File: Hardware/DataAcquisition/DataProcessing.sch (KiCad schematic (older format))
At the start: 36 parts, among them J1 Conn_01x04_Female, J2 Conn_01x04_Female, U5 STM32F030K6Tx, Y1 20MHz

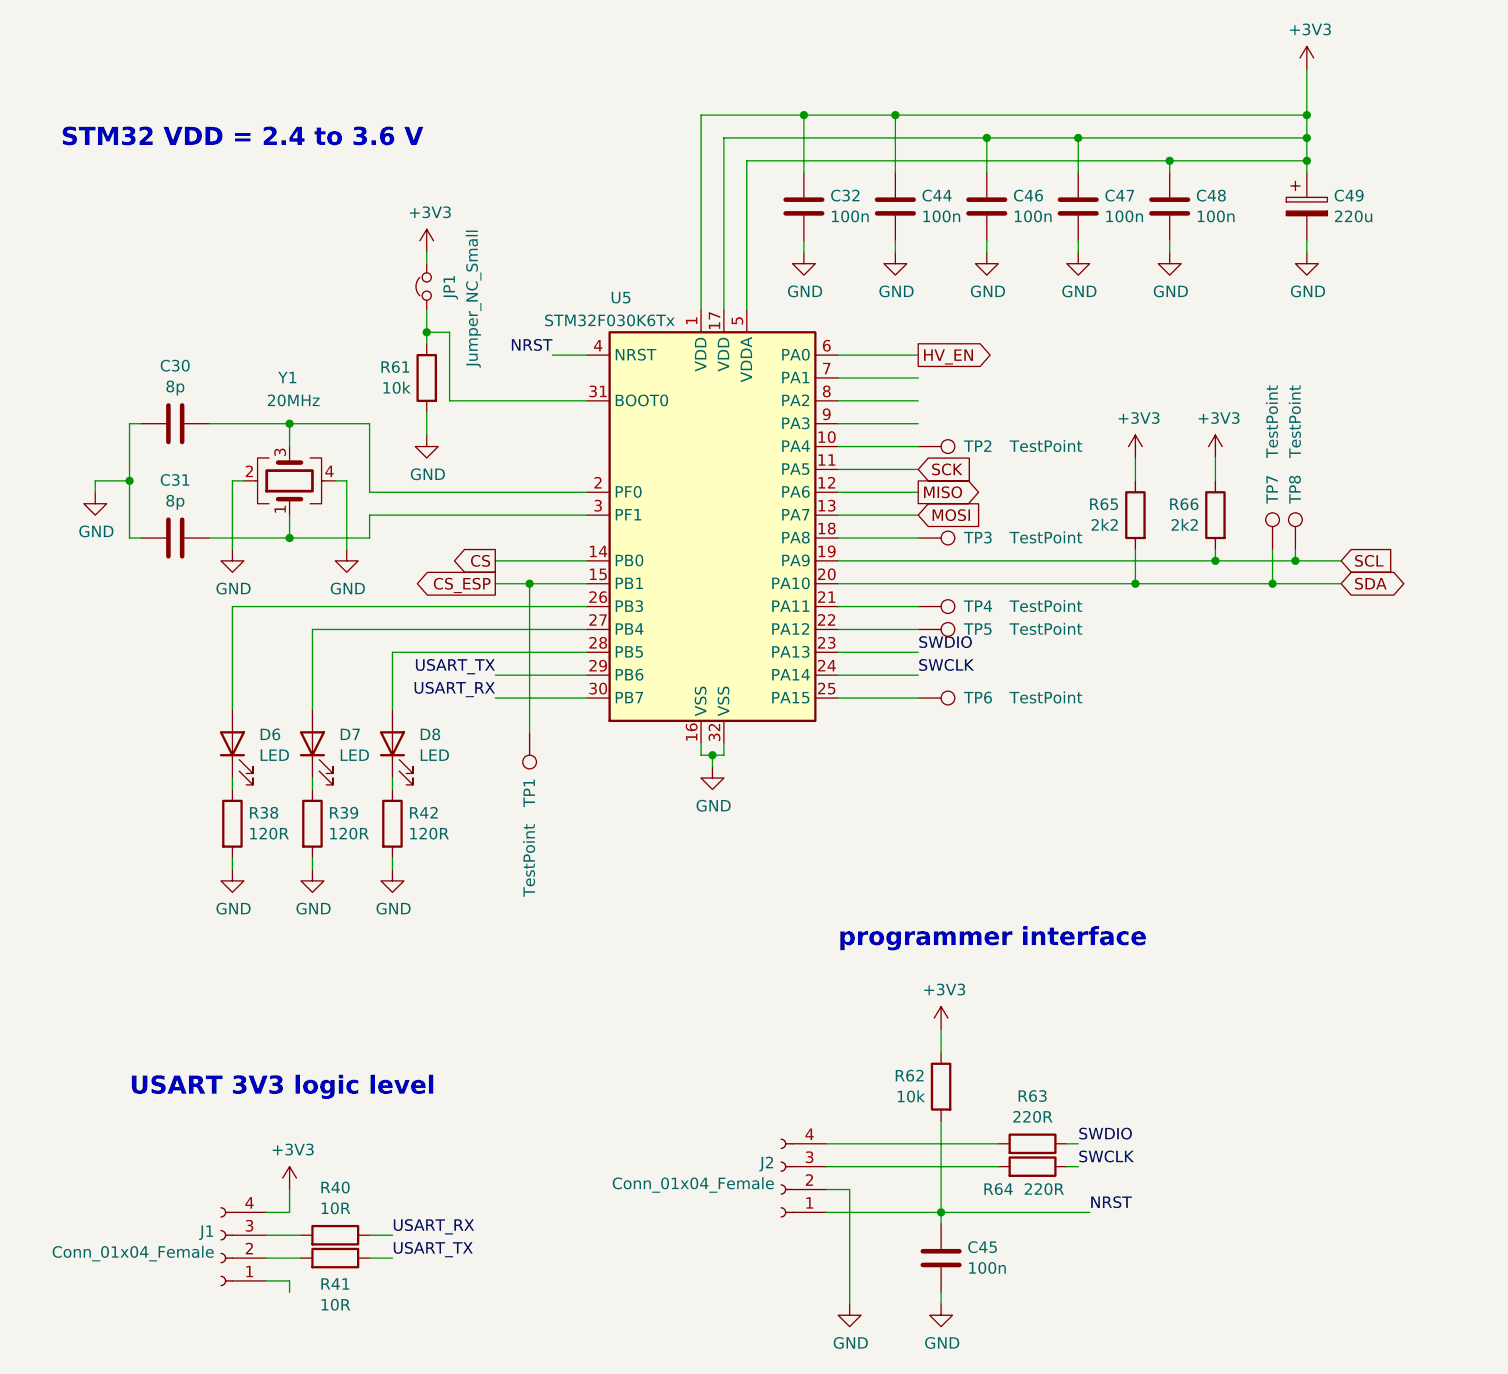
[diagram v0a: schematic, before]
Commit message: split (previousle one) pcb project to three separate pcbs
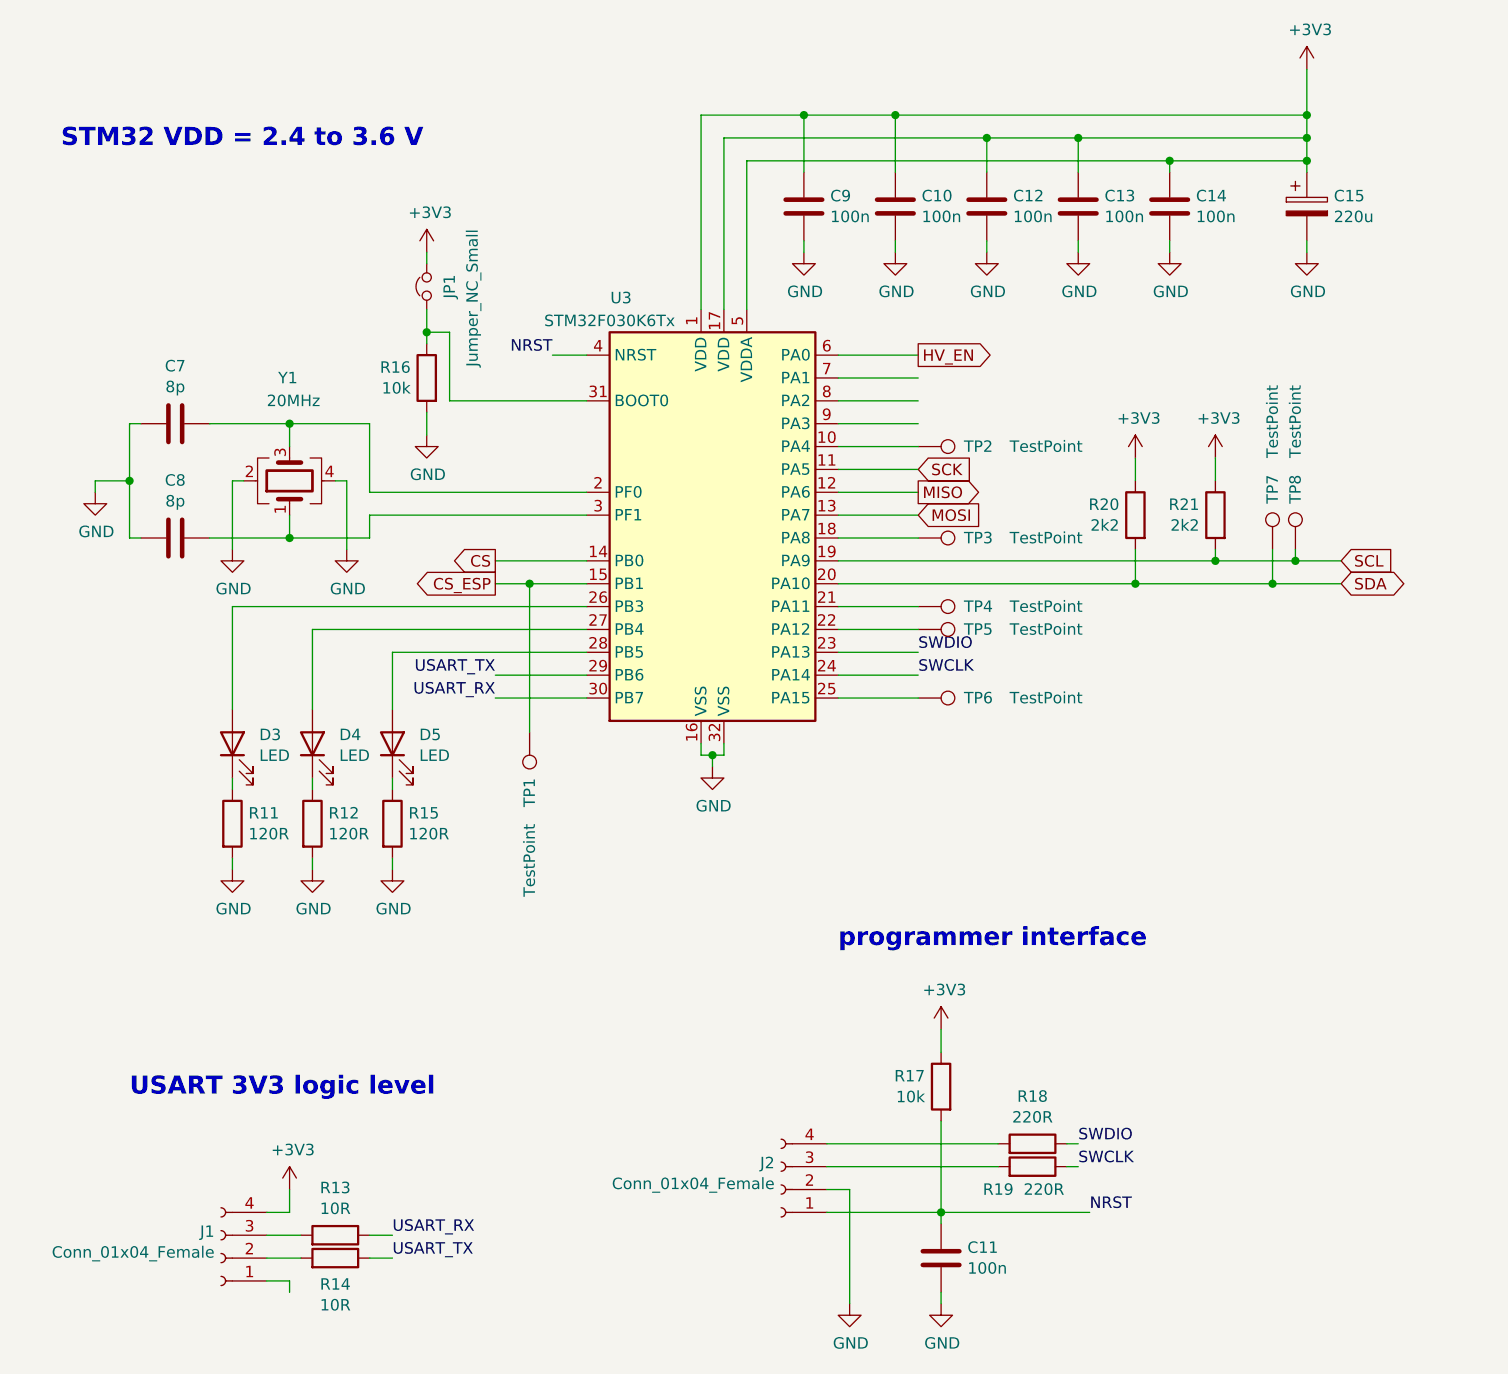
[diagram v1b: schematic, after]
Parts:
- renumbered C44 to C10, C45 to C11, C46 to C12, C47 to C13, C48 to C14, C49 to C15, C30 to C7, C31 to C8, C32 to C9, D6 to D3, D7 to D4, D8 to D5, R38 to R11, R39 to R12, R40 to R13, R41 to R14, R42 to R15, R61 to R16, R62 to R17, R63 to R18, R64 to R19, R65 to R20, R66 to R21, U5 to U3

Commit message: Clarify architecture of acquisition module (#80), removed obsolete files
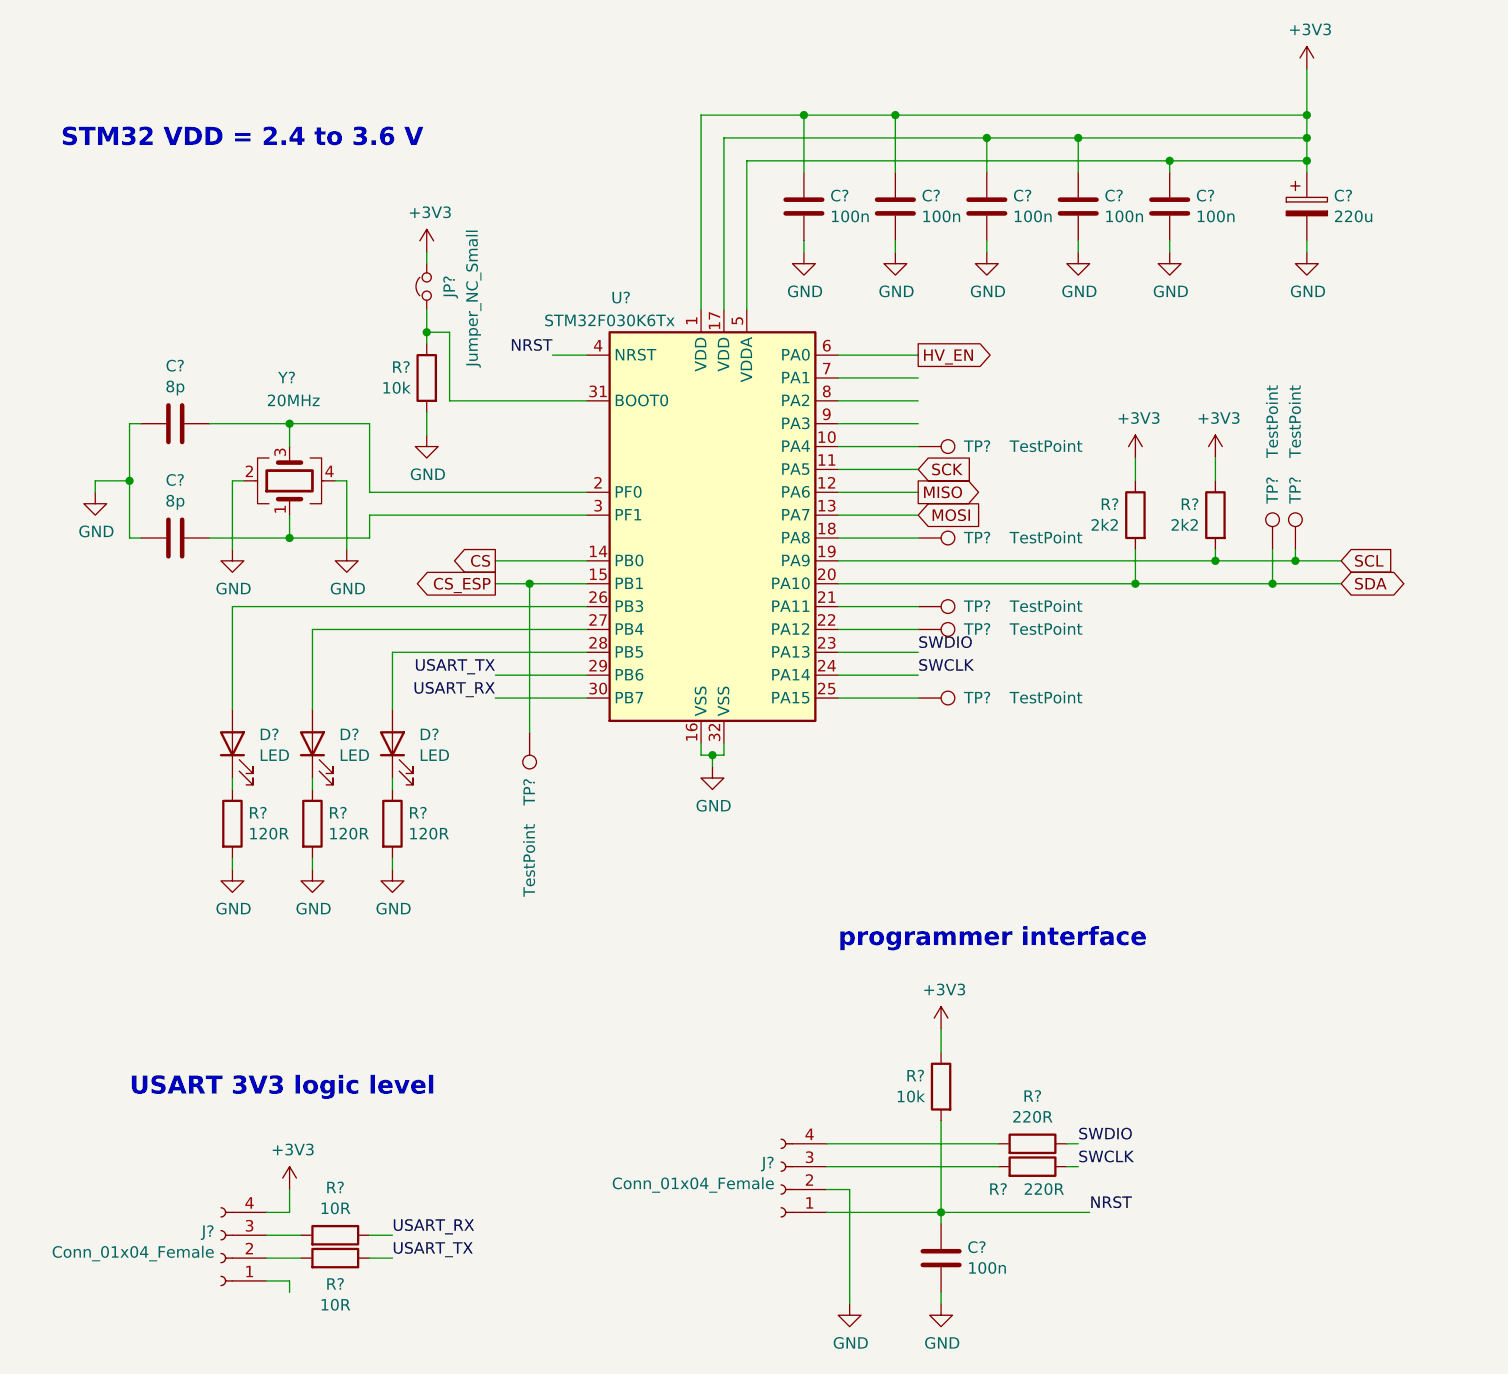
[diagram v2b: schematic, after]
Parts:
- renumbered C15 to C?, J1 to J?, J2 to J?, JP1 to JP?, TP7 to TP?, TP8 to TP?, TP5 to TP?, TP4 to TP?, TP3 to TP?, TP2 to TP?, TP1 to TP?, TP6 to TP?, U3 to U?, Y1 to Y?

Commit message: Rework (in progress) of HV Power Supply due to change topology to flyback (#91), added part of calcuations of components and draft of the circuit. Clarified ducumentation about used mcu. Added footprints for adc and mcu.
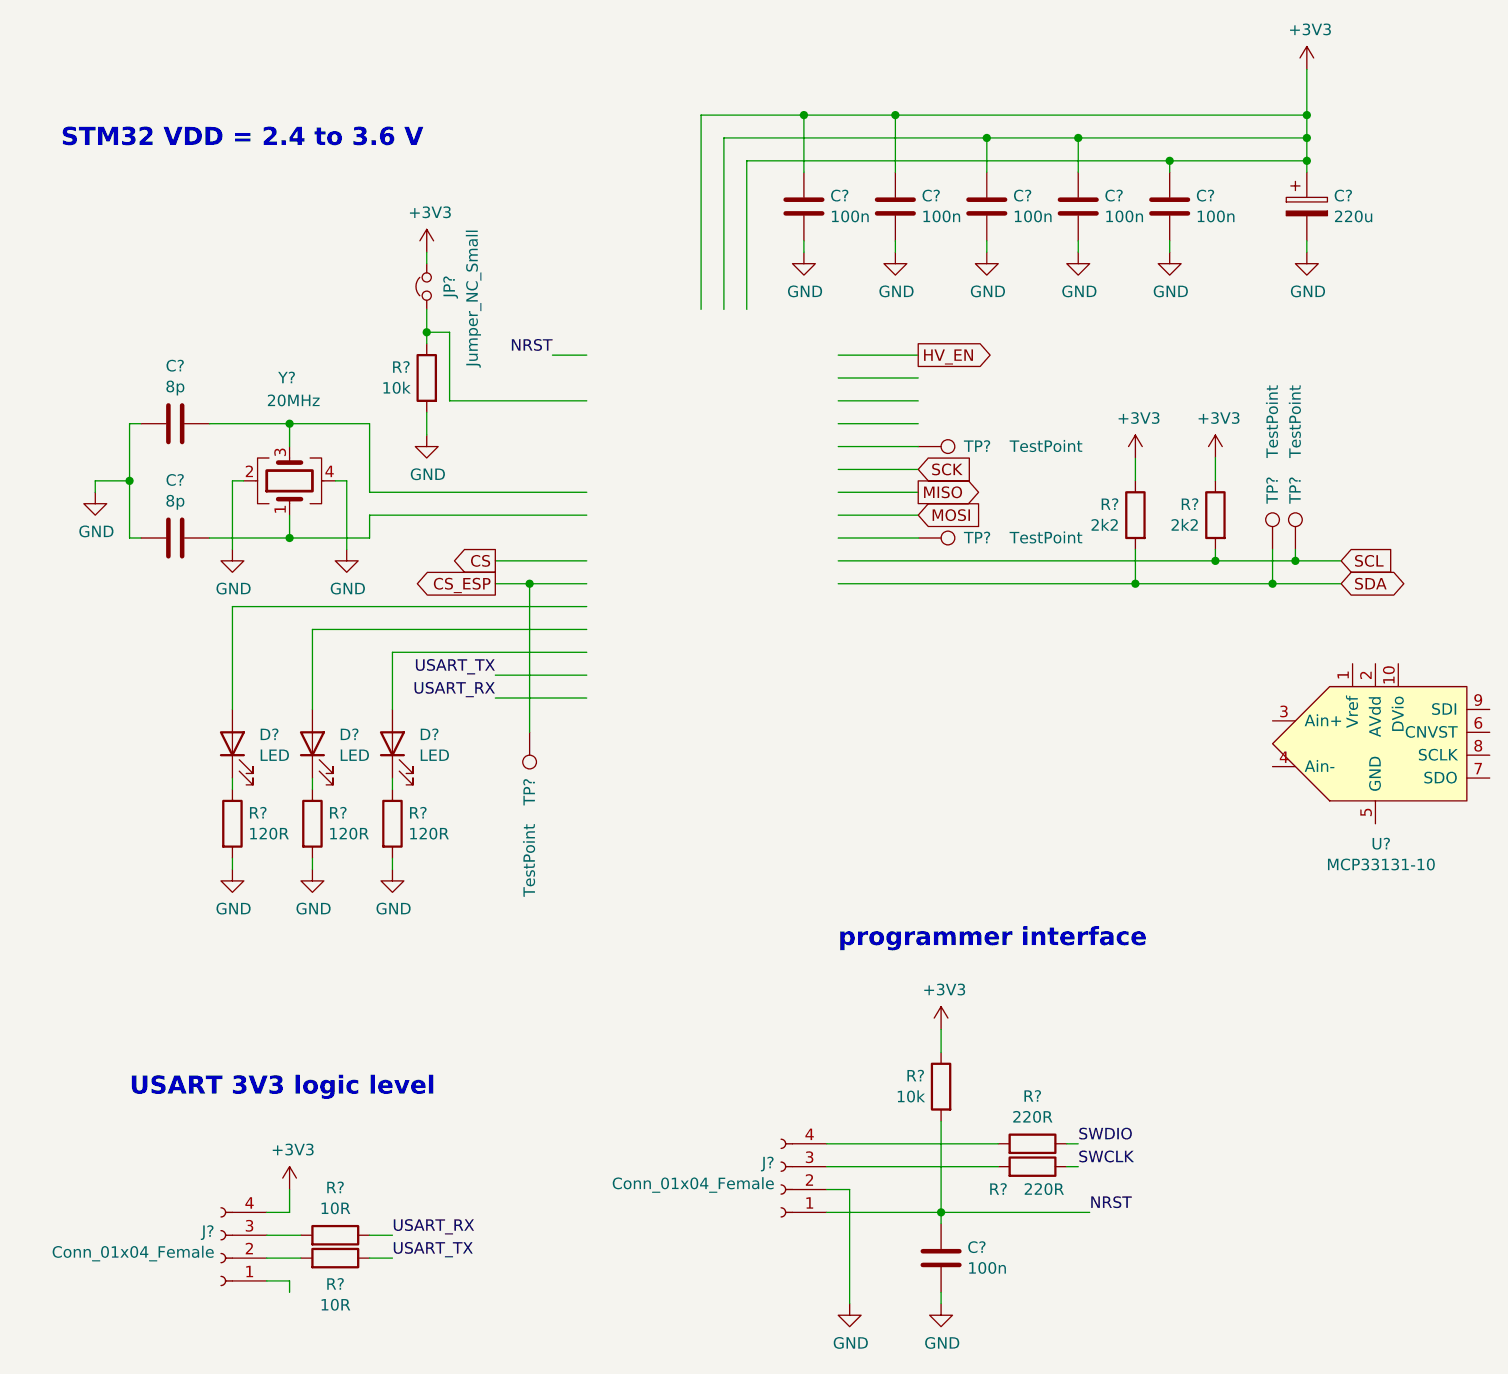
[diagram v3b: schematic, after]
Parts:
- removed TP? (x3): TestPoint, TestPoint:TestPoint_Pad_D1.0mm, symbol Connector:TestPoint
- removed U?: STM32F030K6Tx, Package_QFP:LQFP-32_7x7mm_P0.8mm, symbol MCU_ST_STM32F0:STM32F030K6Tx
- added U?: MCP33131-10, Package_SO:MSOP-10_3x3mm_P0.5mm, symbol DataAcquisition:MCP33131-10
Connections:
- wire segments 123 -> 113
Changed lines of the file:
@@
 $Descr A4 11693 8268
 encoding utf-8
-Sheet 3 3
+Sheet 3 4
 Title "EEG signal processing"
 Date ""
@@
 	1    0    0    -1
 $EndComp
-Wire Wire Line
-	3600 4850 3600 4900
-Wire Wire Line
-	3600 4900 3650 4900
-Wire Wire Line
-	3700 4900 3700 4850
-Wire Wire Line
-	3650 4950 3650 4900
-Connection ~ 3650 4900
-Wire Wire Line
-	3650 4900 3700 4900
 Wire Wire Line
 	4050 2700 4050 2650
@@
 Wire Wire Line
 	4200 3650 4550 3650
-Wire Wire Line
-	4200 4550 4550 4550
 Connection ~ 5850 4050
 Wire Wire Line
@@
 	4200 4150 5500 4150
 Wire Wire Line
-	4550 4350 4200 4350
-Wire Wire Line
-	4550 4250 4200 4250
-Wire Wire Line
 	4550 3950 4200 3950
-Wire Wire Line
-	4200 4450 4550 4450
 Wire Wire Line
 	4550 3150 4200 3150
@@
 	0    1    -1   0
 $EndComp
-Text Label 4550 4450 0    50   ~ 0
-SWDIO
-Text Label 4550 4550 0    50   ~ 0
-SWCLK
 Text Label 5250 6700 0    50   ~ 0
 SWCLK
@@
 Text GLabel 4550 3750 2    50   Output ~ 0
 MISO
-$Comp
-L MCU_ST_STM32F0:STM32F030K6Tx U?
-U 1 1 5DC98A9F
-P 3700 3850
-F 0 "U?" H 3250 4800 50  0000 C CNN
-F 1 "STM32F030K6Tx" H 3200 4700 50  0000 C CNN
-F 2 "Package_QFP:LQFP-32_7x7mm_P0.8mm" H 3200 2950 50  0001 R CNN
-F 3 "http://www.st.com/st-web-ui/static/active/en/resource/technical/document/datasheet/DM00088500.pdf" H 3700 3850 50  0001 C CNN
-	1    3700 3850
-	1    0    0    -1
-$EndComp
 Text Notes 800  2250 0    79   ~ 16
 STM32 VDD = 2.4 to 3.6 V
@@
 $Comp
 L Connector:TestPoint TP?
-U 1 1 5F0F4B62
-P 4550 4350
-F 0 "TP?" V 4550 4550 50  0000 L CNN
-F 1 "TestPoint" V 4550 4750 50  0000 L CNN
-F 2 "TestPoint:TestPoint_Pad_D1.0mm" H 4750 4350 50  0001 C CNN
-F 3 "~" H 4750 4350 50  0001 C CNN
-	1    4550 4350
-	0    1    1    0
-$EndComp
-$Comp
-L Connector:TestPoint TP?
-U 1 1 5F0F5518
-P 4550 4250
-F 0 "TP?" V 4550 4450 50  0000 L CNN
-F 1 "TestPoint" V 4550 4650 50  0000 L CNN
-F 2 "TestPoint:TestPoint_Pad_D1.0mm" H 4750 4250 50  0001 C CNN
-F 3 "~" H 4750 4250 50  0001 C CNN
-	1    4550 4250
-	0    1    1    0
-$EndComp
-$Comp
-L Connector:TestPoint TP?
 U 1 1 5F0F5A50
 P 4550 3950
@@
 $Comp
 L Connector:TestPoint TP?
-U 1 1 5F1139DC
-P 4550 4650
-F 0 "TP?" V 4550 4850 50  0000 L CNN
-F 1 "TestPoint" V 4550 5050 50  0000 L CNN
-F 2 "TestPoint:TestPoint_Pad_D1.0mm" H 4750 4650 50  0001 C CNN
-F 3 "~" H 4750 4650 50  0001 C CNN
-	1    4550 4650
-	0    1    1    0
-$EndComp
-Wire Wire Line
-	4200 4650 4550 4650
-$Comp
-L Connector:TestPoint TP?
 U 1 1 5F0DAD75
 P 6200 4000
@@
 $Comp
 L power:GND #PWR?
-U 1 1 5F14090B
-P 3650 4950
-F 0 "#PWR?" H 3650 4700 50  0001 C CNN
-F 1 "GND" H 3655 4777 50  0000 C CNN
-F 2 "" H 3650 4950 50  0001 C CNN
-F 3 "" H 3650 4950 50  0001 C CNN
-	1    3650 4950
-	1    0    0    -1
-$EndComp
-$Comp
-L power:GND #PWR?
 U 1 1 5F146141
 P 950 3750
@@
 Text GLabel 4550 3150 2    50   Output ~ 0
 HV_EN
+$Comp
+L DataAcquisition:MCP33131-10 U?
+U 1 1 5FB16C07
+P 6550 4850
+F 0 "U?" H 6575 4411 50  0000 C CNN
+F 1 "MCP33131-10" H 6575 4320 50  0000 C CNN
+F 2 "Package_SO:MSOP-10_3x3mm_P0.5mm" H 6950 5150 50  0001 C CNN
+F 3 "https://www.tme.eu/Document/a5a4283a1bfa7721eddf2e7bc5de5352/MCP33131-MCP33121-MCP33111.pdf" H 6950 5150 50  0001 C CNN
+	1    6550 4850
+	1    0    0    -1
+$EndComp
 $EndSCHEMATC
